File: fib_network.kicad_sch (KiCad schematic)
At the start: 0 parts

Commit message: added several ICs, implementted schematics for charger, boost converter and LDOs
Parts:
- added J3: Bus_M.2_Socket_E, symbol Connector:Bus_M.2_Socket_E
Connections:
- new net: J3.1 (GND), J3.18 (GND), J3.33 (GND), J3.39 (GND), J3.45 (GND), J3.51 (GND), J3.57 (GND), J3.63 (GND), J3.69 (GND), J3.7 (GND), J3.75 (GND)
- new net: J3.2 (3.3V), J3.4 (3.3V), J3.72 (3.3V), J3.74 (3.3V)
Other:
- note added: "ETHERNET"
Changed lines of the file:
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@@
 	(generator_version "8.0")
 	(paper "A4")
+	(text "ETHERNET"
+		(exclude_from_sim no)
+		(at 43.942 151.638 0)
+		(effects
+			(font
+				(size 1.27 1.27)
+			)
+		)
+	)
+	(symbol
+		(lib_id "Connector:Bus_M.2_Socket_E")
+		(at 62.23 78.74 0)
+		(unit 1)
+		(exclude_from_sim no)
+		(in_bom yes)
+		(on_board yes)
+		(dnp no)
+		(fields_autoplaced yes)
+		(property "Reference" "J3"
+			(at 64.4241 27.94 0)
+			(effects
+				(font
+					(size 1.27 1.27)
+				)
+				(justify left)
+			)
+		)
+		(property "Value" "Bus_M.2_Socket_E"
+			(at 64.4241 30.48 0)
+			(effects
+				(font
+					(size 1.27 1.27)
+				)
+				(justify left)
+			)
+		)
+		(property "Footprint" ""
+			(at 62.23 52.07 0)
+			(effects
+				(font
+					(size 1.27 1.27)
+				)
+				(hide yes)
+			)
+		)
+		(property "Datasheet" "http://read.pudn.com/downloads794/doc/project/3133918/PCIe_M.2_Electromechanical_Spec_Rev1.0_Final_11012013_RS_Clean.pdf#page=150"
+			(at 62.23 52.07 0)
+			(effects
+				(font
+					(size 1.27 1.27)
+				)
+				(hide yes)
+			)
+		)
+		(property "Description" "M.2 Socket 1-SD Mechanical Key E"
+			(at 62.23 78.74 0)
+			(effects
+				(font
+					(size 1.27 1.27)
+				)
+				(hide yes)
+			)
+		)
+		(pin "19"
+		)
+		(pin "63"
+		)
+		(pin "64"
+		)
+		(pin "65"
+		)
+		(pin "12"
+		)
+		(pin "23"
+		)
+		(pin "3"
+		)
+		(pin "47"
+		)
+		(pin "48"
+		)
+		(pin "66"
+		)
+		(pin "67"
+		)
+		(pin "68"
+		)
+		(pin "6"
+		)
+		(pin "60"
+		)
+		(pin "50"
+		)
+		(pin "51"
+		)
+		(pin "49"
+		)
+		(pin "5"
+		)
+		(pin "8"
+		)
+		(pin "9"
+		)
+		(pin "36"
+		)
+		(pin "37"
+		)
+		(pin "54"
+		)
+		(pin "55"
+		)
+		(pin "18"
+		)
+		(pin "21"
+		)
+		(pin "22"
+		)
+		(pin "32"
+		)
+		(pin "33"
+		)
+		(pin "11"
+		)
+		(pin "58"
+		)
+		(pin "59"
+		)
+		(pin "15"
+		)
+		(pin "17"
+		)
+		(pin "43"
+		)
+		(pin "44"
+		)
+		(pin "56"
+		)
+		(pin "57"
+		)
+		(pin "45"
+		)
+		(pin "46"
+		)
+		(pin "61"
+		)
+		(pin "62"
+		)
+		(pin "38"
+		)
+		(pin "39"
+		)
+		(pin "1"
+		)
+		(pin "2"
+		)
+		(pin "20"
+		)
+		(pin "14"
+		)
+		(pin "16"
+		)
+		(pin "34"
+		)
+		(pin "35"
+		)
+		(pin "52"
+		)
+		(pin "53"
+		)
+		(pin "4"
+		)
+		(pin "40"
+		)
+		(pin "41"
+		)
+		(pin "42"
+		)
+		(pin "10"
+		)
+		(pin "13"
+		)
+		(pin "69"
+		)
+		(pin "7"
+		)
+		(pin "70"
+		)
+		(pin "71"
+		)
+		(pin "72"
+		)
+		(pin "73"
+		)
+		(pin "74"
+		)
+		(pin "75"
+		)
+		(instances
+			(project "Fibel2"
+				(path "/862c21e2-7ec9-4f80-a33c-aad02ea9423e/afa85234-73ed-4fc7-9570-87e781c133e5"
+					(reference "J3")
+					(unit 1)
+				)
+			)
+		)
+	)
 )

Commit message: added symbol&footprint for orin/sodimm, added a bunch of specs and docs, partially implemented audio, full steam ahead
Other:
- moved on the sheet: J3
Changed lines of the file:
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@@
 	(symbol
 		(lib_id "Connector:Bus_M.2_Socket_E")
-		(at 62.23 78.74 0)
+		(at 86.36 81.28 0)
 		(unit 1)
 		(exclude_from_sim no)
@@
 		(fields_autoplaced yes)
 		(property "Reference" "J3"
-			(at 64.4241 27.94 0)
+			(at 88.5541 30.48 0)
 			(effects
 				(font
@@
 		)
 		(property "Value" "Bus_M.2_Socket_E"
-			(at 64.4241 30.48 0)
+			(at 88.5541 33.02 0)
 			(effects
 				(font
@@
 		)
 		(property "Footprint" ""
-			(at 62.23 52.07 0)
+			(at 86.36 54.61 0)
 			(effects
 				(font
@@
 		)
 		(property "Datasheet" "http://read.pudn.com/downloads794/doc/project/3133918/PCIe_M.2_Electromechanical_Spec_Rev1.0_Final_11012013_RS_Clean.pdf#page=150"
-			(at 62.23 52.07 0)
+			(at 86.36 54.61 0)
 			(effects
 				(font
@@
 		)
 		(property "Description" "M.2 Socket 1-SD Mechanical Key E"
-			(at 62.23 78.74 0)
+			(at 86.36 81.28 0)
 			(effects
 				(font

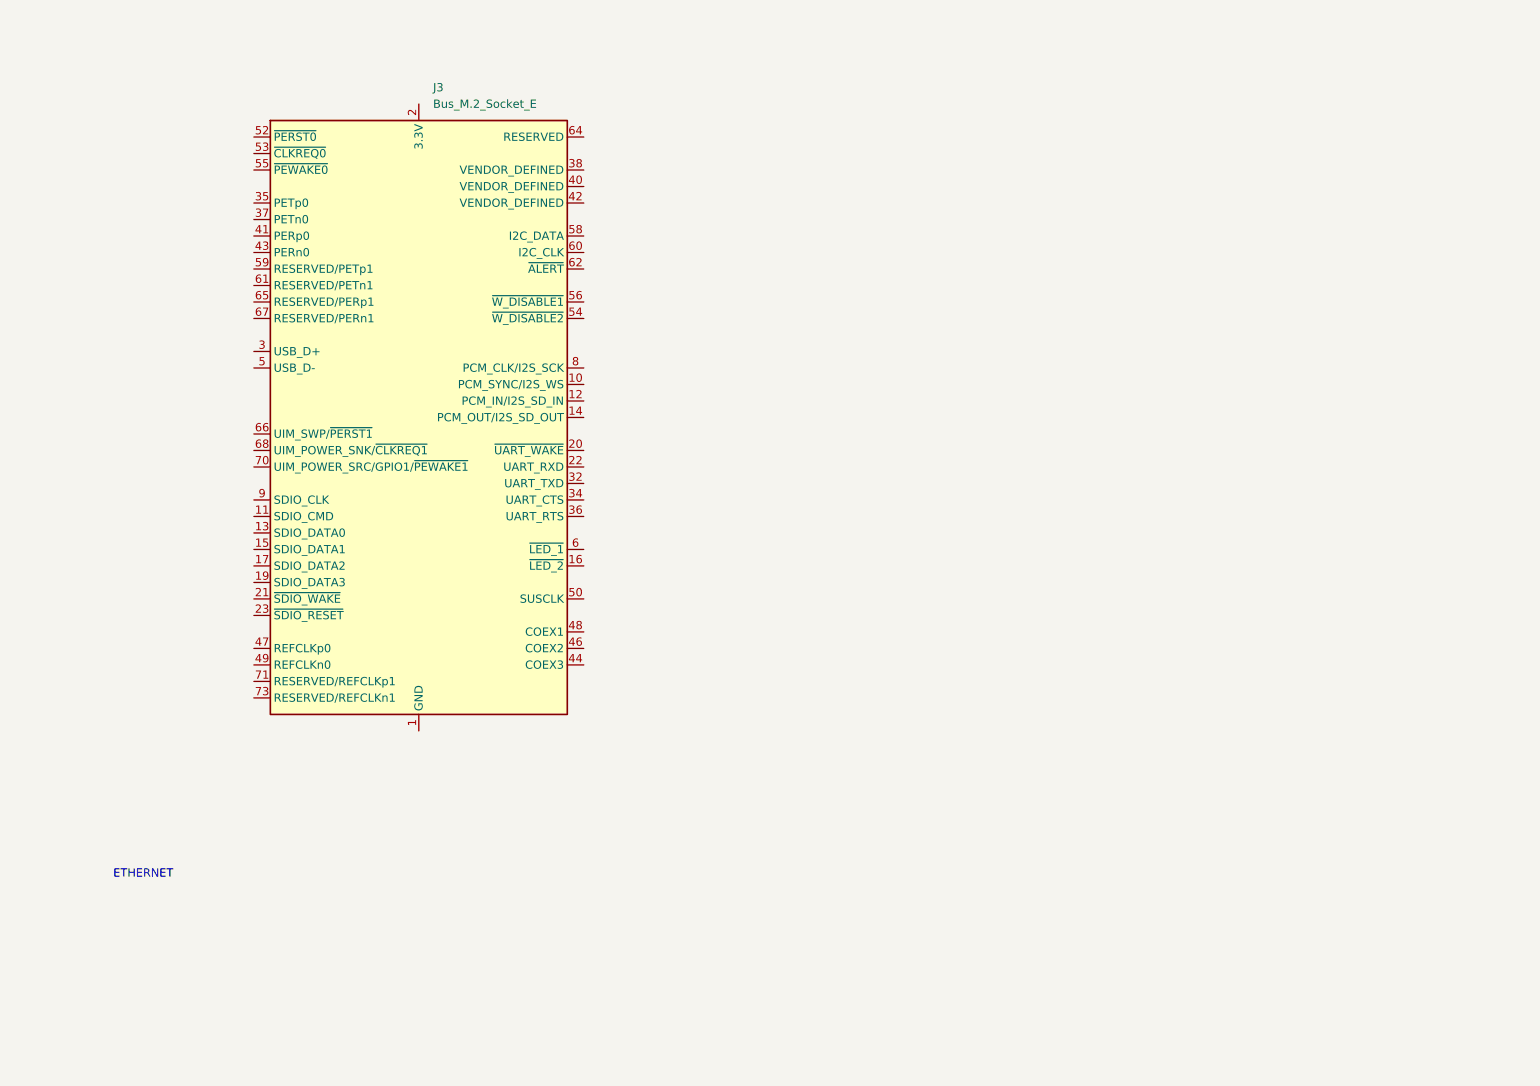
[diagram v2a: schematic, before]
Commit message: added usb+PD+DP & pcie implementations from antmicro design, added specs for USB components, rethought power+usb arch
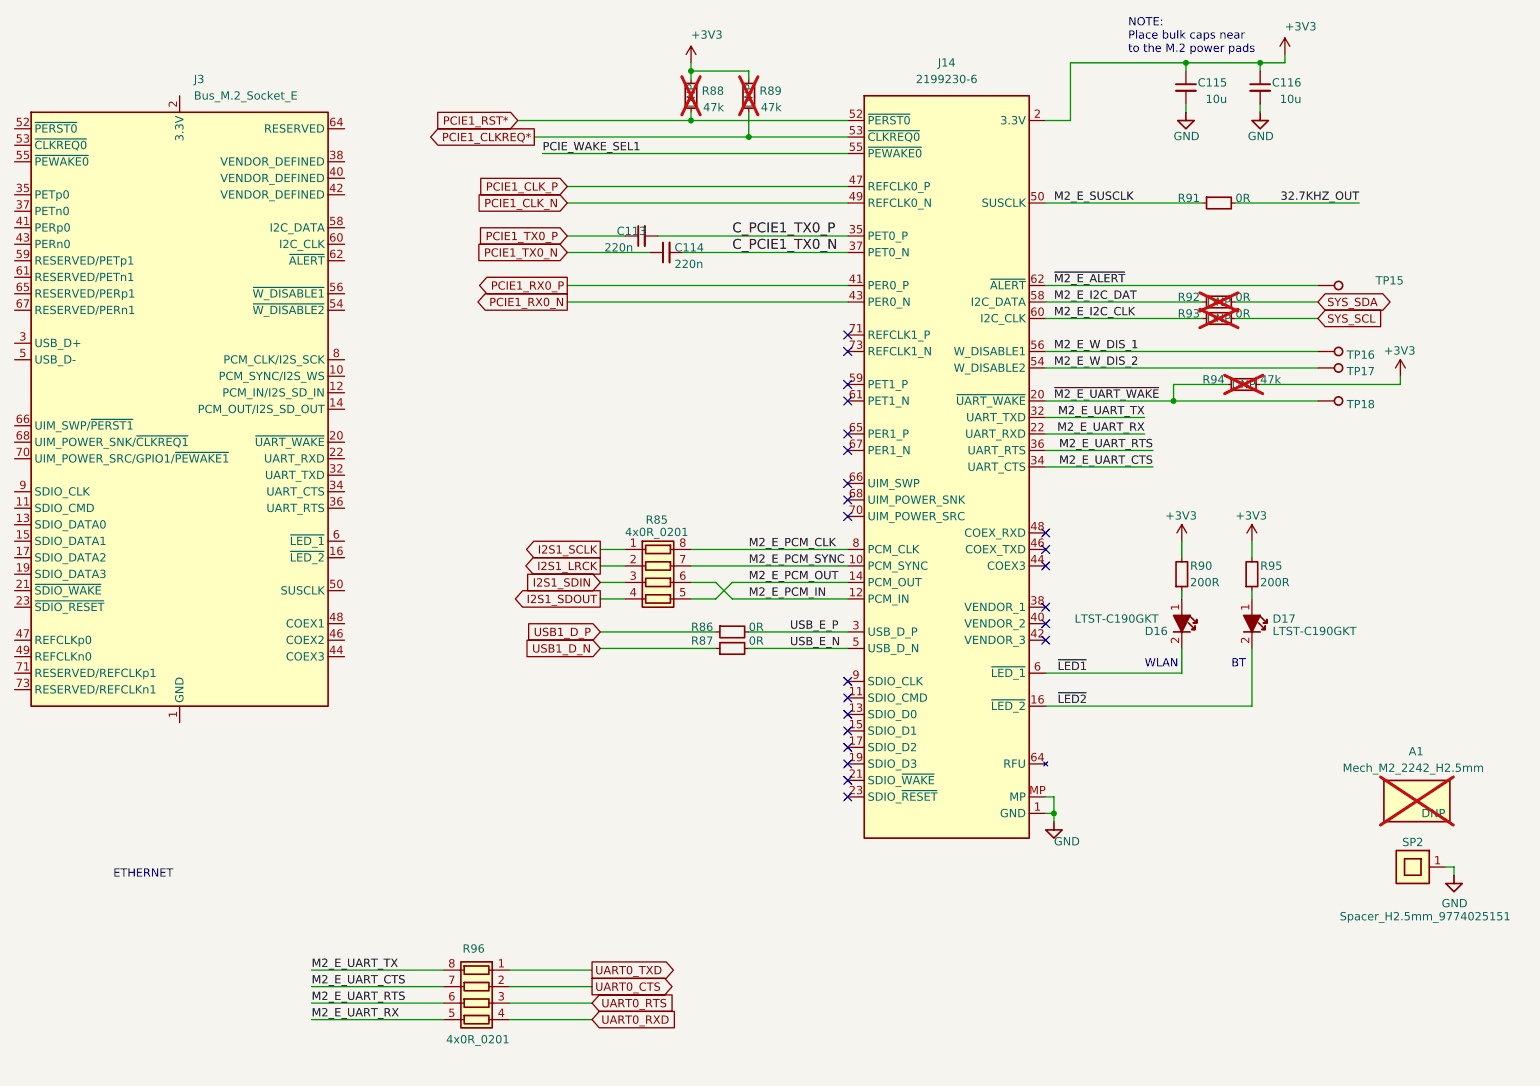
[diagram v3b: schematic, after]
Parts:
- added A1: Mech_M2_2242_H2.5mm, jetson-orin-baseboard-footprints:Mech_M2_2242_H2.5mm, symbol jetson-orin-baseboard:Mech_M2_2242_H2.5mm
- added C113, C114: C_220n_0402, jetson-orin-baseboard-footprints:C_0402_1005Metric, symbol jetson-orin-baseboard:C_220n_0402
- added C115, C116: C_10u_0603, jetson-orin-baseboard-footprints:C_0603_1608Metric, symbol jetson-orin-baseboard:C_10u_0603
- added D16, D17: LED_G_0603_LTST-C190GKT, jetson-orin-baseboard-footprints:LED_0603_1608Metric_G, symbol jetson-orin-baseboard:LED_G_0603_LTST-C190GKT
- added J14: Bus_M.2_2199230-6, jetson-orin-baseboard-footprints:Bus_M.2_Socket_Key_E_TE_2199230-6, symbol jetson-orin-baseboard:Bus_M.2_2199230-6
- added R85, R96: R_4x0R_0201_array, jetson-orin-baseboard-footprints:R_Array_4x0201_Panasonic_EXB18V, symbol jetson-orin-baseboard:R_4x0R_0201_array
- added R86, R87, R91, R92, R93: R_0R_0402, jetson-orin-baseboard-footprints:R_0402_1005Metric, symbol jetson-orin-baseboard:R_0R_0402
- added R88, R89, R94: R_47k_0402, jetson-orin-baseboard-footprints:R_0402_1005Metric, symbol jetson-orin-baseboard:R_47k_0402
- added R90, R95: R_200R_0402, jetson-orin-baseboard-footprints:R_0402_1005Metric, symbol jetson-orin-baseboard:R_200R_0402
- added SP2: Spacer_H2.5mm_9774025151, jetson-orin-baseboard-footprints:Spacer_Drill3.7mm_H2.5mm_9774025151R, symbol jetson-orin-baseboard:Spacer_Drill3.7mm_H2.5mm_9774025151R
- added TP15, TP16, TP17, TP18: TP_0.75mm_SMD, jetson-orin-baseboard-footprints:TP_SMD_0.75mm, symbol jetson-orin-baseboard:TP_0.75mm_SMD
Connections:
- new net: D17.1, R95.1
- new net: D16.1, R90.1
- new net +3V3: C115.1, C116.1, J14.2 (3.3V), J14.4 (3.3V), J14.72 (3.3V), J14.74 (3.3V), R88.1, R89.1, R90.2, R94.2, R95.2
- new net 32.7KHZ_OUT: R91.2
- new net C_PCIE1_TX0_N: C114.2, J14.37 (PET0_N)
- new net C_PCIE1_TX0_P: C113.2, J14.35 (PET0_P)
- new net GND: C115.2, C116.2, J14.1 (GND), J14.18 (GND), J14.33 (GND), J14.39 (GND), J14.45 (GND), J14.51 (GND), J14.57 (GND), J14.63 (GND), J14.69 (GND), J14.7 (GND), J14.75 (GND), J14.MP, SP2.1
- new net I2S1_LRCK: R85.2 (R2.1)
- new net I2S1_SCLK: R85.1 (R1.1)
- new net I2S1_SDIN: R85.3 (R3.1)
- new net I2S1_SDOUT: R85.4 (R4.1)
- new net M2_E_I2C_CLK: J14.60 (I2C_CLK), R93.1
- new net M2_E_I2C_DAT: J14.58 (I2C_DATA), R92.1
- new net M2_E_PCM_CLK: J14.8 (PCM_CLK), R85.8 (R1.2)
- new net M2_E_PCM_IN: J14.12 (PCM_IN), R85.6 (R3.2)
- new net M2_E_PCM_OUT: J14.14 (PCM_OUT), R85.5 (R4.2)
- new net M2_E_PCM_SYNC: J14.10 (PCM_SYNC), R85.7 (R2.2)
- new net M2_E_SUSCLK: J14.50 (SUSCLK), R91.1
- new net M2_E_UART_CTS: J14.34 (UART_CTS), R96.7 (R2.2)
- new net M2_E_UART_RTS: J14.36 (UART_RTS), R96.6 (R3.2)
- new net M2_E_UART_RX: J14.22 (UART_RXD), R96.5 (R4.2)
- new net M2_E_UART_TX: J14.32 (UART_TXD), R96.8 (R1.2)
- new net M2_E_W_DIS_1: J14.56 (W_DISABLE1), TP16.1
- new net M2_E_W_DIS_2: J14.54 (W_DISABLE2), TP17.1
- new net PCIE1_CLKREQ*: J14.53 (~{CLKREQ0}), R89.2
- new net PCIE1_CLK_N: J14.49 (REFCLK0_N)
- new net PCIE1_CLK_P: J14.47 (REFCLK0_P)
- new net PCIE1_RST*: J14.52 (~{PERST0}), R88.2
- new net PCIE1_RX0_N: J14.43 (PER0_N)
- new net PCIE1_RX0_P: J14.41 (PER0_P)
- new net PCIE1_TX0_N: C114.1
- new net PCIE1_TX0_P: C113.1
- new net PCIE_WAKE_SEL1: J14.55 (~{PEWAKE0})
- new net SYS_SCL: R93.2
- new net SYS_SDA: R92.2
- new net UART0_CTS: R96.2 (R2.1)
- new net UART0_RTS: R96.3 (R3.1)
- new net UART0_RXD: R96.4 (R4.1)
- new net UART0_TXD: R96.1 (R1.1)
- new net USB1_D_N: R87.1
- new net USB1_D_P: R86.1
- new net USB_E_N: J14.5 (USB_D_N), R87.2
- new net USB_E_P: J14.3 (USB_D_P), R86.2
- new net ~{LED1}: D16.2, J14.6 (~{LED_1})
- new net ~{LED2}: D17.2, J14.16 (~{LED_2})
- new net ~{M2_E_ALERT}: J14.62 (~{ALERT}), TP15.1
- new net ~{M2_E_UART_WAKE}: J14.20 (~{UART_WAKE}), R94.1, TP18.1
- no-connect marks 0 -> 23
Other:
- note added: "BT"
- note added: "NOTE: Place bulk caps near to the M.2 power pads"
- note added: "WLAN"
- moved on the sheet: J3

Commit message: added nets for 40 pin headers (epd & rpi header) connected some of the nets i'm reeusing
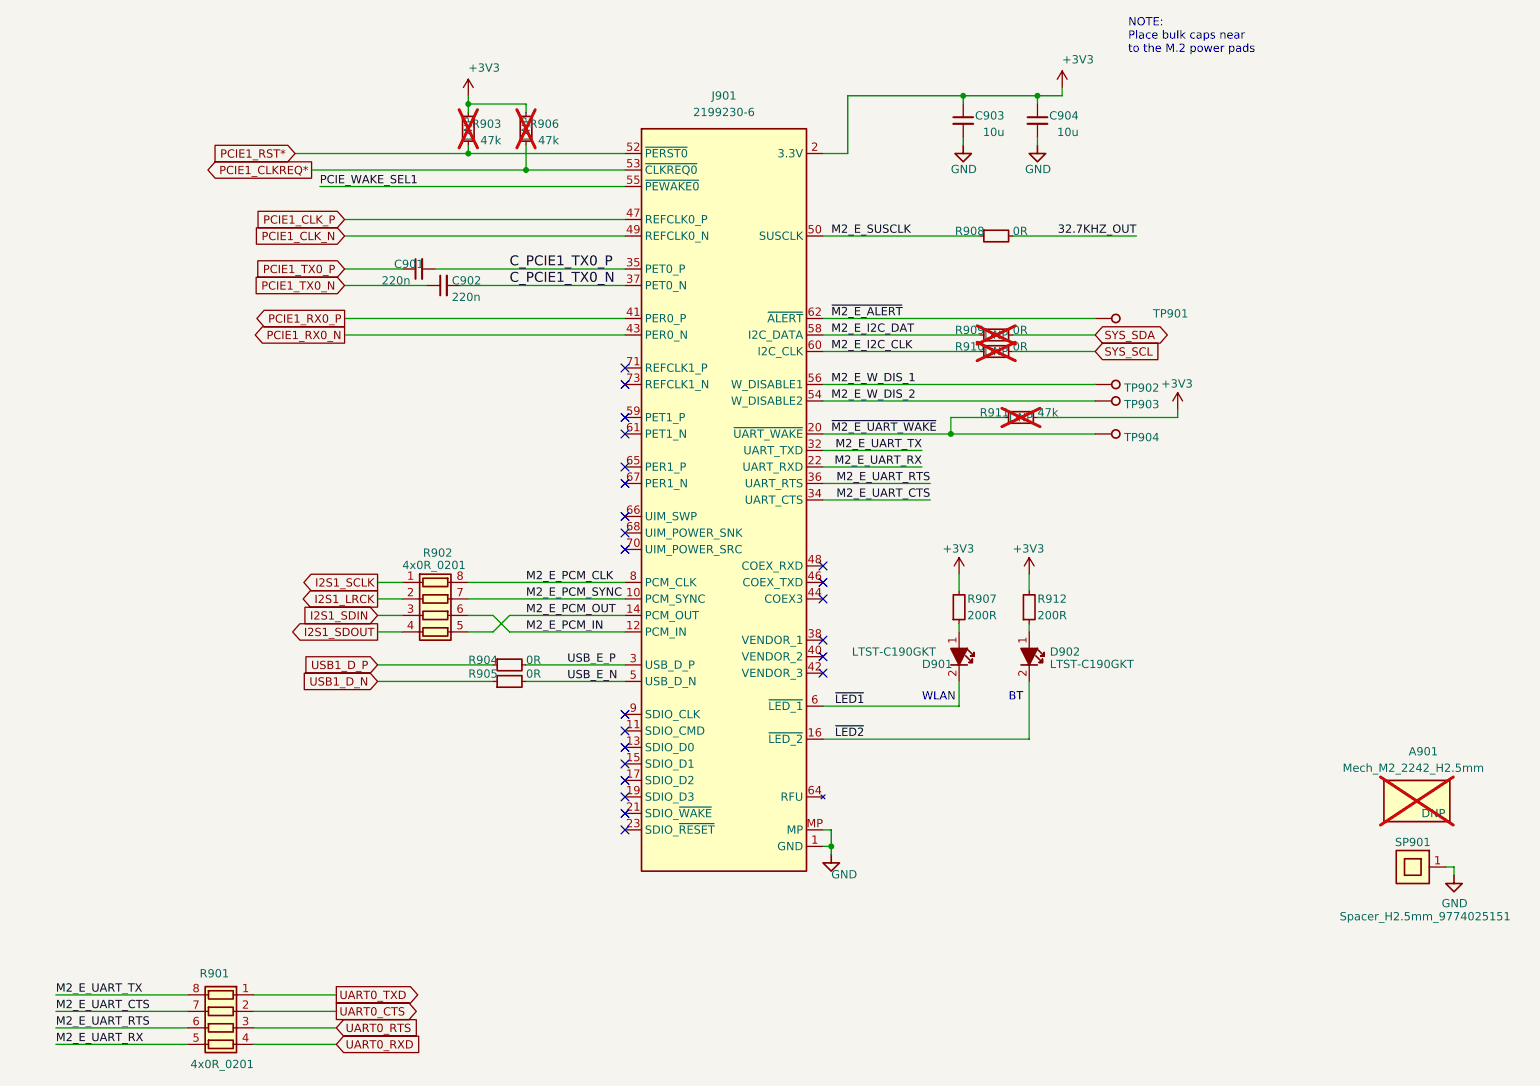
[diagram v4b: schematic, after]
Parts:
- removed J3: Bus_M.2_Socket_E, symbol Connector:Bus_M.2_Socket_E
- C901: renamed from C113; value C_220n_0402 -> 220nF; footprint jetson-orin-baseboard-footprints:C_0402_1005Metric -> Capacitor_SMD:C_0603_1608Metric
- C902: renamed from C114; value C_220n_0402 -> 220nF; footprint jetson-orin-baseboard-footprints:C_0402_1005Metric -> Capacitor_SMD:C_0603_1608Metric
- C903: renamed from C115; value C_10u_0603 -> 20uF; footprint jetson-orin-baseboard-footprints:C_0603_1608Metric -> Capacitor_SMD:C_0603_1608Metric
- C904: renamed from C116; value C_10u_0603 -> 20uF; footprint jetson-orin-baseboard-footprints:C_0603_1608Metric -> Capacitor_SMD:C_0603_1608Metric
- R903: renamed from R88; value R_47k_0402 -> 47K; footprint jetson-orin-baseboard-footprints:R_0402_1005Metric -> Resistor_SMD:R_0603_1608Metric
- R904: renamed from R86; value R_0R_0402 -> 0R; footprint jetson-orin-baseboard-footprints:R_0402_1005Metric -> Resistor_SMD:R_0603_1608Metric
- R905: renamed from R87; value R_0R_0402 -> 0R; footprint jetson-orin-baseboard-footprints:R_0402_1005Metric -> Resistor_SMD:R_0603_1608Metric
- R906: renamed from R89; value R_47k_0402 -> 47K; footprint jetson-orin-baseboard-footprints:R_0402_1005Metric -> Resistor_SMD:R_0603_1608Metric
- R907: renamed from R90; value R_200R_0402 -> 200R; footprint jetson-orin-baseboard-footprints:R_0402_1005Metric -> Resistor_SMD:R_0603_1608Metric
- R908: renamed from R91; value R_0R_0402 -> 0R; footprint jetson-orin-baseboard-footprints:R_0402_1005Metric -> Resistor_SMD:R_0603_1608Metric
- R909: renamed from R92; value R_0R_0402 -> 0R; footprint jetson-orin-baseboard-footprints:R_0402_1005Metric -> Resistor_SMD:R_0603_1608Metric
- R910: renamed from R93; value R_0R_0402 -> 0R; footprint jetson-orin-baseboard-footprints:R_0402_1005Metric -> Resistor_SMD:R_0603_1608Metric
- R911: renamed from R94; value R_47k_0402 -> 47K; footprint jetson-orin-baseboard-footprints:R_0402_1005Metric -> Resistor_SMD:R_0603_1608Metric
- R912: renamed from R95; value R_200R_0402 -> 200R; footprint jetson-orin-baseboard-footprints:R_0402_1005Metric -> Resistor_SMD:R_0603_1608Metric
- TP901: renamed from TP15; footprint jetson-orin-baseboard-footprints:TP_SMD_0.75mm -> TestPoint:TestPoint_Pad_D1.0mm
- TP902: renamed from TP16; footprint jetson-orin-baseboard-footprints:TP_SMD_0.75mm -> TestPoint:TestPoint_Pad_D1.0mm
- TP903: renamed from TP17; footprint jetson-orin-baseboard-footprints:TP_SMD_0.75mm -> TestPoint:TestPoint_Pad_D1.0mm
- TP904: renamed from TP18; footprint jetson-orin-baseboard-footprints:TP_SMD_0.75mm -> TestPoint:TestPoint_Pad_D1.0mm
- renumbered A1 to A901, D16 to D901, D17 to D902, J14 to J901, R96 to R901, R85 to R902, SP2 to SP901
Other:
- note removed: "ETHERNET"
- moved on the sheet: C901, C902, C903, C904, D901, D902, J901, R901, R902, R903, R904, R905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
